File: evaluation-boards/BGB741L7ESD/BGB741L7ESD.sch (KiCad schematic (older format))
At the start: 22 parts, among them J1 CONN_01X01, J2 CONN_01X01, J3 CONN_01X03, J4 CONN_COAXIAL, J5 CONN_COAXIAL, J6 CONN_COAXIAL, J7 CONN_COAXIAL, U1 BGB741L7ESD

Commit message: update BGB741L7ESD to KiCad 5.1
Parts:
- C1, C2, C3, C4, C5, C6, C7, C8, C9: symbol C -> Device:C
- J1, J2: symbol CONN_01X01 -> Connector_Generic:Conn_01x01
- J3: symbol CONN_01X03 -> Connector_Generic:Conn_01x03
- J4, J5, J6, J7: symbol CONN_COAXIAL -> Connector:Conn_Coaxial
- L1, L2, L3, L4: symbol L -> Device:L
- R1: symbol R -> Device:R
- U1: symbol BGB741L7ESD -> gsg-symbols:BGB741L7ESD
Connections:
- wire segments 43 -> 51
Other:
- moved on the sheet: J4, J5, J6, J7
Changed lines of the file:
@@
-EESchema Schematic File Version 2
-LIBS:power
-LIBS:device
-LIBS:transistors
-LIBS:conn
-LIBS:linear
-LIBS:regul
-LIBS:74xx
-LIBS:cmos4000
-LIBS:adc-dac
-LIBS:memory
-LIBS:xilinx
-LIBS:microcontrollers
-LIBS:dsp
-LIBS:microchip
-LIBS:analog_switches
-LIBS:motorola
-LIBS:texas
-LIBS:intel
-LIBS:audio
-LIBS:interface
-LIBS:digital-audio
-LIBS:philips
-LIBS:display
-LIBS:cypress
-LIBS:siliconi
-LIBS:opto
-LIBS:atmel
-LIBS:contrib
-LIBS:valves
-LIBS:gsg-symbols
-LIBS:BGB741L7ESD-cache
-EELAYER 25 0
+EESchema Schematic File Version 4
+EELAYER 30 0
 EELAYER END
 $Descr A4 11693 8268
@@
 $EndDescr
 $Comp
-L CONN_COAXIAL J5
+L Connector:Conn_Coaxial J5
 U 1 1 5BCE48F3
 P 8000 3400
@@
 $EndComp
 $Comp
-L CONN_COAXIAL J4
+L Connector:Conn_Coaxial J4
 U 1 1 5BCE498F
 P 3950 3400
@@
 $EndComp
 $Comp
-L BGB741L7ESD U1
+L gsg-symbols:BGB741L7ESD U1
 U 1 1 5BCE4B07
 P 6250 3300
@@
 $EndComp
 $Comp
-L C C2
+L Device:C C2
 U 1 1 5BCE4BA2
 P 7600 3400
@@
 $EndComp
 $Comp
-L C C1
+L Device:C C1
 U 1 1 5BCE4C25
 P 4350 3400
@@
 $EndComp
 $Comp
-L L L2
+L Device:L L2
 U 1 1 5BCE4D52
 P 7350 3650
@@
 $EndComp
 $Comp
-L C C4
+L Device:C C4
 U 1 1 5BCE4E0B
 P 7350 4150
@@
 $EndComp
 $Comp
-L GND #PWR01
+L power:GND #PWR01
 U 1 1 5BCE4E6D
 P 7350 4400
@@
 $EndComp
 $Comp
-L VCC #PWR02
+L power:VCC #PWR02
 U 1 1 5BCE4EC0
 P 7450 3900
@@
 $EndComp
 Wire Wire Line
-	7350 3800 7350 4000
+	7350 3800 7350 3900
 Wire Wire Line
 	7350 3900 7450 3900
@@
 	7350 3500 7350 3400
 Wire Wire Line
-	6900 3400 7450 3400
+	6900 3400 7350 3400
 Connection ~ 7350 3400
 $Comp
-L L L1
+L Device:L L1
 U 1 1 5BCE4F6B
 P 4950 3300
@@
 	4700 3300 4700 3400
 Wire Wire Line
-	4500 3400 5600 3400
+	4500 3400 4700 3400
 Connection ~ 4700 3400
 $Comp
-L C C3
+L Device:C C3
 U 1 1 5BCE5088
 P 5200 3650
@@
 $EndComp
 $Comp
-L GND #PWR03
+L power:GND #PWR03
 U 1 1 5BCE508E
 P 5200 3900
@@
 	5200 3800 5200 3900
 Wire Wire Line
-	5100 3300 5600 3300
+	5100 3300 5200 3300
 Wire Wire Line
 	5200 3300 5200 3500
 Connection ~ 5200 3300
 $Comp
-L VCC #PWR04
+L power:VCC #PWR04
 U 1 1 5BCE50D9
 P 5200 3150
@@
 	5200 3150 5200 3200
 Wire Wire Line
-	5200 3200 5600 3200
-$Comp
-L GND #PWR05
+	5200 3200 5500 3200
+$Comp
+L power:GND #PWR05
 U 1 1 5BCE5119
 P 6250 2600
@@
 	6250 2600 6250 2700
 $Comp
-L R R1
+L Device:R R1
 U 1 1 5BCE5191
 P 7000 2950
@@
 $EndComp
 $Comp
-L VCC #PWR06
+L power:VCC #PWR06
 U 1 1 5BCE521C
 P 7000 2700
@@
 	7350 3300 7350 2150
 $Comp
-L GND #PWR07
+L power:GND #PWR07
 U 1 1 5BCE537E
 P 8000 3700
@@
 $EndComp
 $Comp
-L GND #PWR08
+L power:GND #PWR08
 U 1 1 5BCE53A7
 P 3950 3700
@@
 	7750 3400 7850 3400
 $Comp
-L CONN_01X03 J3
+L Connector_Generic:Conn_01x03 J3
 U 1 1 5BCE5466
 P 7350 1950
@@
 $EndComp
 $Comp
-L VCC #PWR09
+L power:VCC #PWR09
 U 1 1 5BCE5546
 P 7250 2250
@@
 $EndComp
 $Comp
-L GND #PWR010
+L power:GND #PWR010
 U 1 1 5BCE559E
 P 7450 2250
@@
 	8000 3600 8000 3700
 $Comp
-L CONN_01X01 J1
+L Connector_Generic:Conn_01x01 J1
 U 1 1 5BCE598B
 P 4500 1900
@@
 $EndComp
 $Comp
-L CONN_01X01 J2
+L Connector_Generic:Conn_01x01 J2
 U 1 1 5BCE5A4E
 P 5150 1900
@@
 $EndComp
 $Comp
-L VCC #PWR011
+L power:VCC #PWR011
 U 1 1 5BCE5AB7
 P 4500 2200
@@
 $EndComp
 $Comp
-L GND #PWR012
+L power:GND #PWR012
 U 1 1 5BCE5AE9
 P 5150 2200
@@
 	5150 2100 5150 2200
 $Comp
-L CONN_COAXIAL J7
+L Connector:Conn_Coaxial J7
 U 1 1 5BCE6011
 P 8000 4850
@@
 $EndComp
 $Comp
-L CONN_COAXIAL J6
+L Connector:Conn_Coaxial J6
 U 1 1 5BCE6017
 P 4050 4850
@@
 $EndComp
 $Comp
-L C C6
+L Device:C C6
 U 1 1 5BCE6023
 P 7600 4850
@@
 $EndComp
 $Comp
-L C C5
+L Device:C C5
 U 1 1 5BCE6029
 P 4450 4850
@@
 $EndComp
 $Comp
-L L L4
+L Device:L L4
 U 1 1 5BCE602F
 P 7350 5100
@@
 $EndComp
 $Comp
-L C C8
+L Device:C C8
 U 1 1 5BCE6035
 P 7350 5600
@@
 $EndComp
 $Comp
-L GND #PWR013
+L power:GND #PWR013
 U 1 1 5BCE603B
 P 7350 5850
@@
 $EndComp
 $Comp
-L VCC #PWR014
+L power:VCC #PWR014
 U 1 1 5BCE6041
 P 7450 5350
@@
 $EndComp
 Wire Wire Line
-	7350 5250 7350 5450
+	7350 5250 7350 5350
 Wire Wire Line
 	7350 5350 7450 5350
@@
 Connection ~ 4800 4850
 $Comp
-L C C7
+L Device:C C7
 U 1 1 5BCE6058
 P 5300 5100
@@
 $EndComp
 $Comp
-L GND #PWR015
+L power:GND #PWR015
 U 1 1 5BCE605E
 P 5300 5350
@@
 	5300 4750 5300 4950
 $Comp
-L GND #PWR016
+L power:GND #PWR016
 U 1 1 5BCE606E
 P 8000 5150
@@
 $EndComp
 $Comp
-L GND #PWR017
+L power:GND #PWR017
 U 1 1 5BCE6074
 P 4050 5150
@@
 	8000 5050 8000 5150
 $Comp
-L L L3
+L Device:L L3
 U 1 1 5BCE604E
 P 5050 4750
@@
 	5200 4750 5300 4750
 Wire Wire Line
-	4600 4850 7450 4850
-$Comp
-L C C9
+	4600 4850 4800 4850
+$Comp
+L Device:C C9
 U 1 1 5BCE58AF
 P 5500 3650
@@
 $EndComp
 $Comp
-L GND #PWR018
+L power:GND #PWR018
 U 1 1 5BCE5ABF
 P 5500 3900
@@
 	5500 3500 5500 3200
 Connection ~ 5500 3200
+Wire Wire Line
+	7350 3900 7350 4000
+Wire Wire Line
+	7350 3400 7450 3400
+Wire Wire Line
+	4700 3400 5600 3400
+Wire Wire Line
+	5200 3300 5600 3300
+Wire Wire Line
+	7350 5350 7350 5450
+Wire Wire Line
+	7350 4850 7450 4850
+Wire Wire Line
+	4800 4850 7350 4850
+Wire Wire Line
+	5500 3200 5600 3200
 $EndSCHEMATC

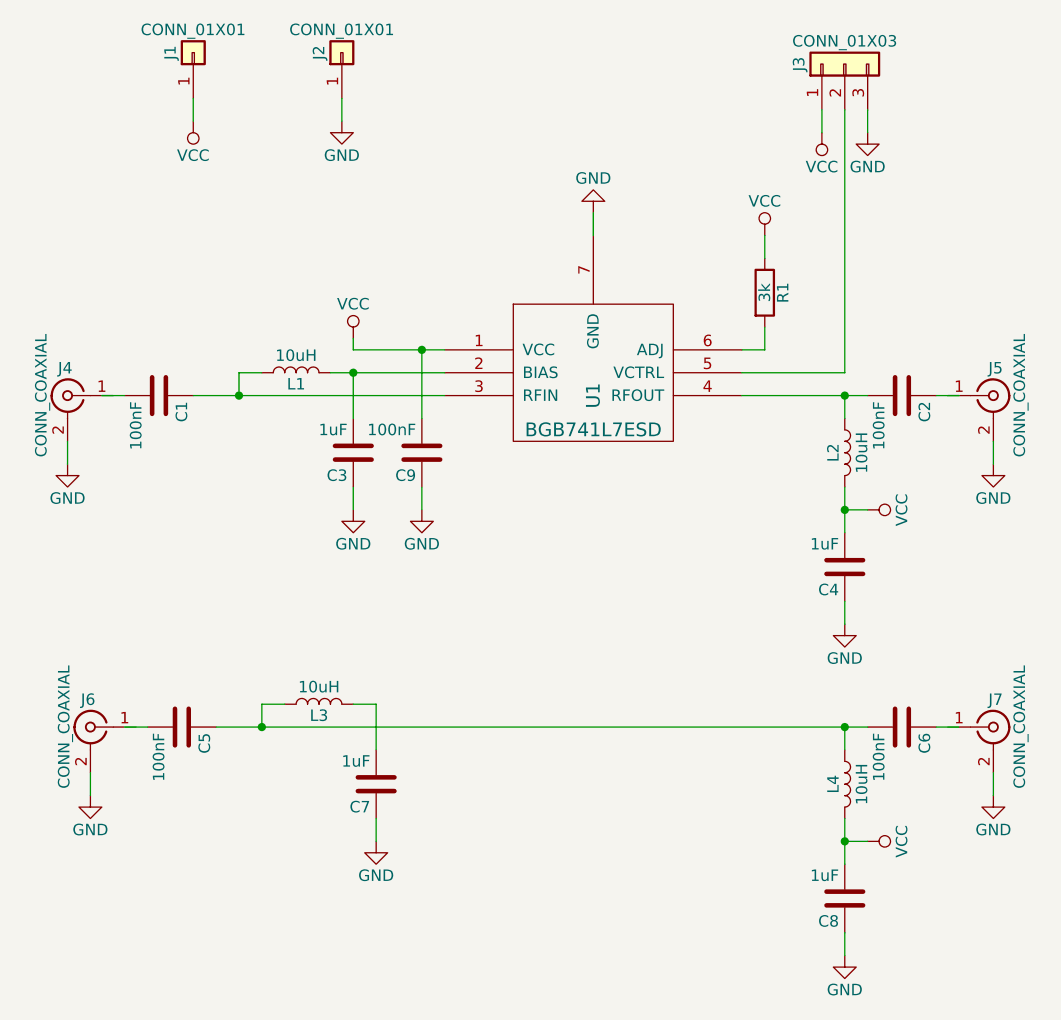
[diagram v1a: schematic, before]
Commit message: BGB741L7ESD: update with PCB edge SMA connectors
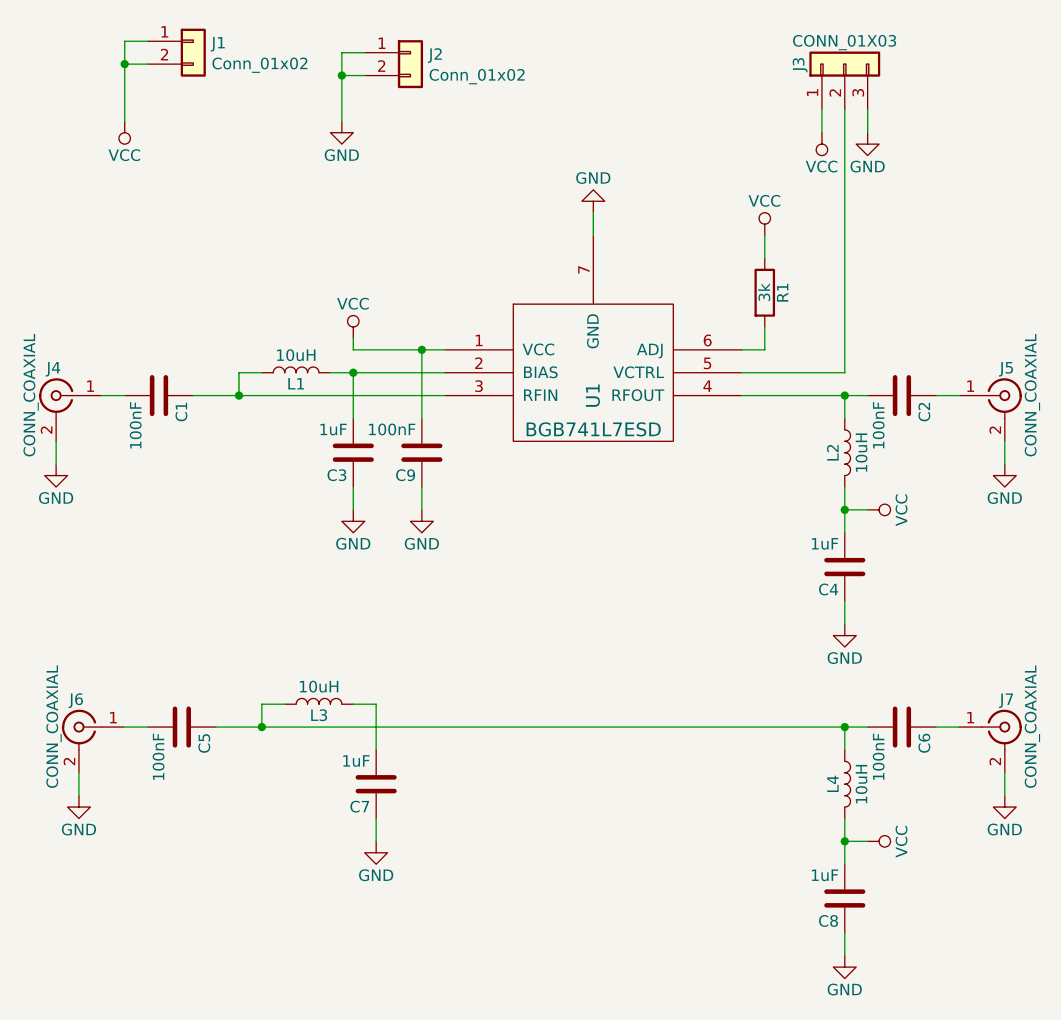
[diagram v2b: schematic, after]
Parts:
- removed J1, J2: CONN_01X01, gsg-modules:HEADER-1x1, symbol Connector_Generic:Conn_01x01
- added J1, J2: Conn_01x02, Connector_PinHeader_2.54mm:PinHeader_1x02_P2.54mm_Vertical, symbol Connector_Generic:Conn_01x02
- J3: footprint gsg-modules:HEADER-1x3 -> Connector_PinHeader_2.54mm:PinHeader_1x03_P2.54mm_Vertical
- J4, J5, J6, J7: footprint gsg-modules:SMA-VERTICAL -> gsg-modules:SMA-73251-2120
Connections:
- wire segments 51 -> 57
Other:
- moved on the sheet: J4, J5, J6, J7
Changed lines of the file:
@@
 L Connector:Conn_Coaxial J5
 U 1 1 5BCE48F3
-P 8000 3400
-F 0 "J5" H 8010 3520 50  0000 C CNN
-F 1 "CONN_COAXIAL" V 8115 3400 50  0000 C CNN
-F 2 "gsg-modules:SMA-VERTICAL" H 8000 3400 50  0001 C CNN
-F 3 "" H 8000 3400 50  0001 C CNN
-	1    8000 3400
+P 8050 3400
+F 0 "J5" H 8060 3520 50  0000 C CNN
+F 1 "CONN_COAXIAL" V 8165 3400 50  0000 C CNN
+F 2 "gsg-modules:SMA-73251-2120" H 8050 3400 50  0001 C CNN
+F 3 "" H 8050 3400 50  0001 C CNN
+	1    8050 3400
 	1    0    0    -1
 $EndComp
@@
 L Connector:Conn_Coaxial J4
 U 1 1 5BCE498F
-P 3950 3400
-F 0 "J4" H 3960 3520 50  0000 C CNN
-F 1 "CONN_COAXIAL" V 4065 3400 50  0000 C CNN
-F 2 "gsg-modules:SMA-VERTICAL" H 3950 3400 50  0001 C CNN
-F 3 "" H 3950 3400 50  0001 C CNN
-	1    3950 3400
+P 3900 3400
+F 0 "J4" H 3910 3520 50  0000 C CNN
+F 1 "CONN_COAXIAL" V 4015 3400 50  0000 C CNN
+F 2 "gsg-modules:SMA-73251-2120" H 3900 3400 50  0001 C CNN
+F 3 "" H 3900 3400 50  0001 C CNN
+	1    3900 3400
 	-1   0    0    -1
 $EndComp
@@
 L power:GND #PWR07
 U 1 1 5BCE537E
-P 8000 3700
-F 0 "#PWR07" H 8000 3450 50  0001 C CNN
-F 1 "GND" H 8000 3550 50  0000 C CNN
-F 2 "" H 8000 3700 50  0001 C CNN
-F 3 "" H 8000 3700 50  0001 C CNN
-	1    8000 3700
+P 8050 3700
+F 0 "#PWR07" H 8050 3450 50  0001 C CNN
+F 1 "GND" H 8050 3550 50  0000 C CNN
+F 2 "" H 8050 3700 50  0001 C CNN
+F 3 "" H 8050 3700 50  0001 C CNN
+	1    8050 3700
 	1    0    0    -1
 $EndComp
@@
 L power:GND #PWR08
 U 1 1 5BCE53A7
-P 3950 3700
-F 0 "#PWR08" H 3950 3450 50  0001 C CNN
-F 1 "GND" H 3950 3550 50  0000 C CNN
-F 2 "" H 3950 3700 50  0001 C CNN
-F 3 "" H 3950 3700 50  0001 C CNN
-	1    3950 3700
-	1    0    0    -1
-$EndComp
-Wire Wire Line
-	3950 3700 3950 3600
+P 3900 3700
+F 0 "#PWR08" H 3900 3450 50  0001 C CNN
+F 1 "GND" H 3900 3550 50  0000 C CNN
+F 2 "" H 3900 3700 50  0001 C CNN
+F 3 "" H 3900 3700 50  0001 C CNN
+	1    3900 3700
+	1    0    0    -1
+$EndComp
+Wire Wire Line
+	3900 3700 3900 3600
 Wire Wire Line
 	4100 3400 4200 3400
@@
 F 0 "J3" H 7350 2150 50  0000 C CNN
 F 1 "CONN_01X03" V 7450 1950 50  0000 C CNN
-F 2 "gsg-modules:HEADER-1x3" H 7350 1950 50  0001 C CNN
+F 2 "Connector_PinHeader_2.54mm:PinHeader_1x03_P2.54mm_Vertical" H 7350 1950 50  0001 C CNN
 F 3 "" H 7350 1950 50  0001 C CNN
 	1    7350 1950
@@
 	7250 2150 7250 2250
 Wire Wire Line
-	8000 3600 8000 3700
-$Comp
-L Connector_Generic:Conn_01x01 J1
-U 1 1 5BCE598B
-P 4500 1900
-F 0 "J1" H 4500 2000 50  0000 C CNN
-F 1 "CONN_01X01" V 4600 1900 50  0000 C CNN
-F 2 "gsg-modules:HEADER-1x1" H 4500 1900 50  0001 C CNN
-F 3 "" H 4500 1900 50  0001 C CNN
-	1    4500 1900
-	0    -1   -1   0
-$EndComp
-$Comp
-L Connector_Generic:Conn_01x01 J2
-U 1 1 5BCE5A4E
-P 5150 1900
-F 0 "J2" H 5150 2000 50  0000 C CNN
-F 1 "CONN_01X01" V 5250 1900 50  0000 C CNN
-F 2 "gsg-modules:HEADER-1x1" H 5150 1900 50  0001 C CNN
-F 3 "" H 5150 1900 50  0001 C CNN
-	1    5150 1900
-	0    -1   -1   0
-$EndComp
+	8050 3600 8050 3700
 $Comp
 L power:VCC #PWR011
 U 1 1 5BCE5AB7
-P 4500 2200
-F 0 "#PWR011" H 4500 2050 50  0001 C CNN
-F 1 "VCC" H 4500 2350 50  0000 C CNN
-F 2 "" H 4500 2200 50  0001 C CNN
-F 3 "" H 4500 2200 50  0001 C CNN
-	1    4500 2200
+P 4200 2200
+F 0 "#PWR011" H 4200 2050 50  0001 C CNN
+F 1 "VCC" H 4200 2350 50  0000 C CNN
+F 2 "" H 4200 2200 50  0001 C CNN
+F 3 "" H 4200 2200 50  0001 C CNN
+	1    4200 2200
 	-1   0    0    1
 $EndComp
@@
 	1    0    0    -1
 $EndComp
-Wire Wire Line
-	4500 2100 4500 2200
-Wire Wire Line
-	5150 2100 5150 2200
 $Comp
 L Connector:Conn_Coaxial J7
 U 1 1 5BCE6011
-P 8000 4850
-F 0 "J7" H 8010 4970 50  0000 C CNN
-F 1 "CONN_COAXIAL" V 8115 4850 50  0000 C CNN
-F 2 "gsg-modules:SMA-VERTICAL" H 8000 4850 50  0001 C CNN
-F 3 "" H 8000 4850 50  0001 C CNN
-	1    8000 4850
+P 8050 4850
+F 0 "J7" H 8060 4970 50  0000 C CNN
+F 1 "CONN_COAXIAL" V 8165 4850 50  0000 C CNN
+F 2 "gsg-modules:SMA-73251-2120" H 8050 4850 50  0001 C CNN
+F 3 "" H 8050 4850 50  0001 C CNN
+	1    8050 4850
 	1    0    0    -1
 $EndComp
@@
 L Connector:Conn_Coaxial J6
 U 1 1 5BCE6017
-P 4050 4850
-F 0 "J6" H 4060 4970 50  0000 C CNN
-F 1 "CONN_COAXIAL" V 4165 4850 50  0000 C CNN
-F 2 "gsg-modules:SMA-VERTICAL" H 4050 4850 50  0001 C CNN
-F 3 "" H 4050 4850 50  0001 C CNN
-	1    4050 4850
+P 4000 4850
+F 0 "J6" H 4010 4970 50  0000 C CNN
+F 1 "CONN_COAXIAL" V 4115 4850 50  0000 C CNN
+F 2 "gsg-modules:SMA-73251-2120" H 4000 4850 50  0001 C CNN
+F 3 "" H 4000 4850 50  0001 C CNN
+	1    4000 4850
 	-1   0    0    -1
 $EndComp
@@
 L power:GND #PWR016
 U 1 1 5BCE606E
-P 8000 5150
-F 0 "#PWR016" H 8000 4900 50  0001 C CNN
-F 1 "GND" H 8000 5000 50  0000 C CNN
-F 2 "" H 8000 5150 50  0001 C CNN
-F 3 "" H 8000 5150 50  0001 C CNN
-	1    8000 5150
+P 8050 5150
+F 0 "#PWR016" H 8050 4900 50  0001 C CNN
+F 1 "GND" H 8050 5000 50  0000 C CNN
+F 2 "" H 8050 5150 50  0001 C CNN
+F 3 "" H 8050 5150 50  0001 C CNN
+	1    8050 5150
 	1    0    0    -1
 $EndComp
@@
 L power:GND #PWR017
 U 1 1 5BCE6074
-P 4050 5150
-F 0 "#PWR017" H 4050 4900 50  0001 C CNN
-F 1 "GND" H 4050 5000 50  0000 C CNN
-F 2 "" H 4050 5150 50  0001 C CNN
-F 3 "" H 4050 5150 50  0001 C CNN
-	1    4050 5150
-	1    0    0    -1
-$EndComp
-Wire Wire Line
-	4050 5150 4050 5050
+P 4000 5150
+F 0 "#PWR017" H 4000 4900 50  0001 C CNN
+F 1 "GND" H 4000 5000 50  0000 C CNN
+F 2 "" H 4000 5150 50  0001 C CNN
+F 3 "" H 4000 5150 50  0001 C CNN
+	1    4000 5150
+	1    0    0    -1
+$EndComp
+Wire Wire Line
+	4000 5150 4000 5050
 Wire Wire Line
 	4200 4850 4300 4850
@@
 	7750 4850 7850 4850
 Wire Wire Line
-	8000 5050 8000 5150
+	8050 5050 8050 5150
 $Comp
 L Device:L L3
@@
 Wire Wire Line
 	5500 3200 5600 3200
+$Comp
+L Connector_Generic:Conn_01x02 J2
+U 1 1 5F36AAD1
+P 5450 1900
+F 0 "J2" H 5530 1892 50  0000 L CNN
+F 1 "Conn_01x02" H 5530 1801 50  0000 L CNN
+F 2 "Connector_PinHeader_2.54mm:PinHeader_1x02_P2.54mm_Vertical" H 5450 1900 50  0001 C CNN
+F 3 "~" H 5450 1900 50  0001 C CNN
+	1    5450 1900
+	1    0    0    -1
+$EndComp
+$Comp
+L Connector_Generic:Conn_01x02 J1
+U 1 1 5F36D977
+P 4500 1850
+F 0 "J1" H 4580 1842 50  0000 L CNN
+F 1 "Conn_01x02" H 4580 1751 50  0000 L CNN
+F 2 "Connector_PinHeader_2.54mm:PinHeader_1x02_P2.54mm_Vertical" H 4500 1850 50  0001 C CNN
+F 3 "~" H 4500 1850 50  0001 C CNN
+	1    4500 1850
+	1    0    0    -1
+$EndComp
+Wire Wire Line
+	5150 2200 5150 2000
+Wire Wire Line
+	5150 1900 5250 1900
+Wire Wire Line
+	5150 2000 5250 2000
+Connection ~ 5150 2000
+Wire Wire Line
+	5150 2000 5150 1900
+Wire Wire Line
+	4200 2200 4200 1950
+Wire Wire Line
+	4200 1850 4300 1850
+Wire Wire Line
+	4200 1950 4300 1950
+Connection ~ 4200 1950
+Wire Wire Line
+	4200 1950 4200 1850
 $EndSCHEMATC
